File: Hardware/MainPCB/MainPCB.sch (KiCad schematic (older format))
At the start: 23 parts, among them Q1 FDS9926A, U1 BQ24075, U2 BQ29700, U3 TLV75533PDBV

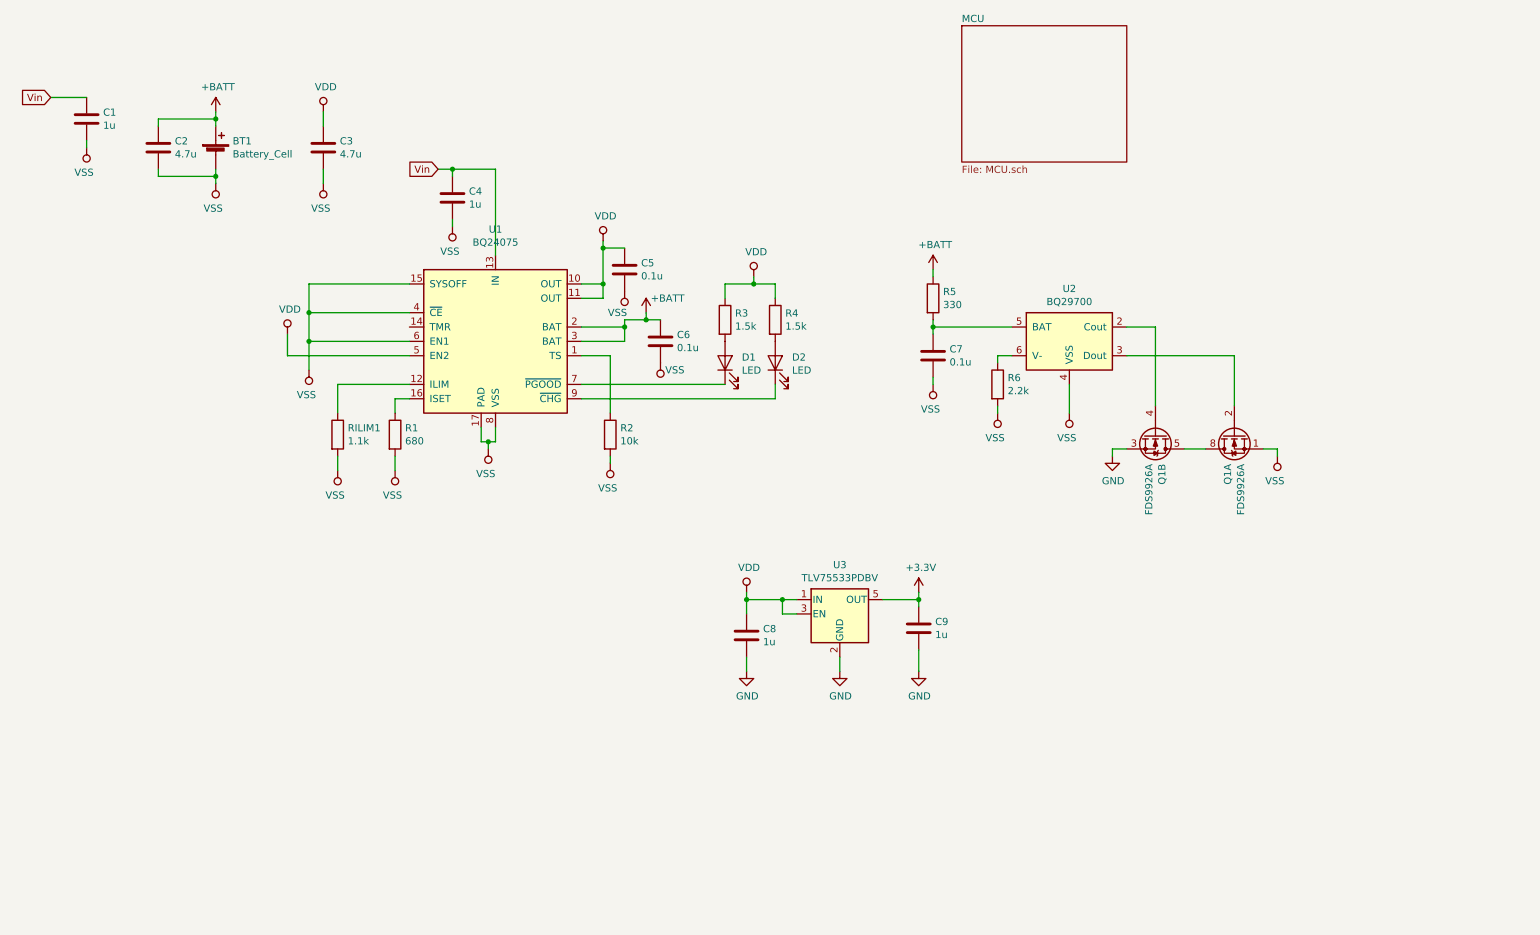
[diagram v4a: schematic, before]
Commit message: Discrete componenten rond IC's en IC's zelfs nagegaan. + toevoeging BOM
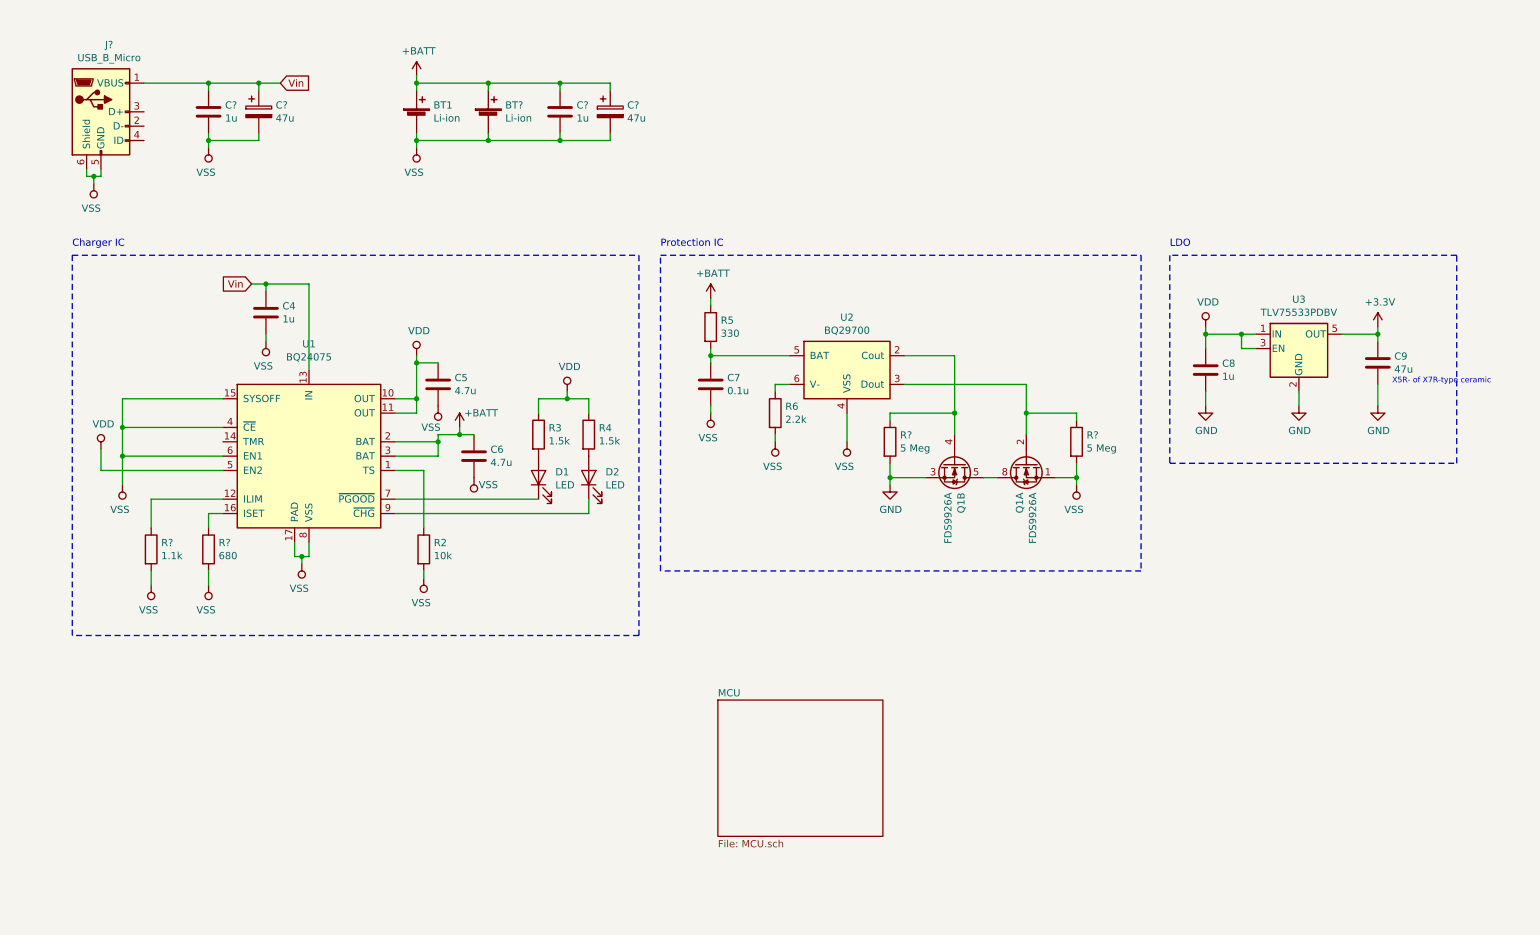
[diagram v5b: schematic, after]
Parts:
- removed C2, C3: 4.7u, symbol Device:C
- added BT?: Li-ion, Battery:BatteryHolder_Keystone_1042_1x18650, symbol Device:Battery_Cell
- added C? (x2): 47u, symbol Device:CP
- added C?: 1u, symbol Device:C
- added J?: USB_B_Micro, Connector_USB:USB_Micro-B_Wuerth_629105150521, symbol Connector:USB_B_Micro
- added R? (x2): 5 Meg, Resistor_SMD:R_0612_1632Metric, symbol Device:R
- BT1: value Battery_Cell -> Li-ion
- C5, C6: value 0.1u -> 4.7u
- C9: value 1u -> 47u
- renumbered C1 to C?, RILIM1 to R?, R1 to R?
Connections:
- net +BATT: now also BT?.1 (+), C?.1, C?.1
- net GND: now also R?.2
- net VSS: now also BT?.2 (-), C?.2, C?.2, C?.2, J?.5 (GND), J?.6 (Shield), R?.2
- net Vin: now also C?.1, J?.1 (VBUS)
- net at Q1.4 (G2), U2.2 (Cout): now also R?.1
- net at Q1.2 (G1), U2.3 (Dout): now also R?.1
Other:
- note added: "Charger IC"
- note added: "LDO"
- note added: "Protection IC"
- note added: "X5R- of X7R-type ceramic"
- moved on the sheet: BT1, C4, C5, C6, C7, C8, C9, C?, D1, D2, Q1A, Q1B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

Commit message: schematic voor esp32 mainboard
de esp toegevoegd en de nodige connecties gemaakt
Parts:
- U3: symbol Regulator_Linear:TLV75533PDBV -> MainPCB-rescue:TLV75533PDBV-Regulator_Linear
- gave numbers to parts that had none: 10
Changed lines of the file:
@@
 EESchema Schematic File Version 4
+LIBS:MainPCB-cache
 EELAYER 30 0
 EELAYER END
@@
 $EndComp
 $Comp
-L Device:R R?
+L Device:R R7
 U 1 1 5E5AB74D
 P 2000 4250
-F 0 "R?" H 2070 4296 50  0000 L CNN
+F 0 "R7" H 2070 4296 50  0000 L CNN
 F 1 "680" H 2070 4205 50  0000 L CNN
 F 2 "Resistor_SMD:R_0612_1632Metric" V 1930 4250 50  0001 C CNN
@@
 	1250 3700 1250 3550
 $Comp
-L Device:R R?
+L Device:R R1
 U 1 1 5E5A99E6
 P 1600 4250
-F 0 "R?" H 1670 4296 50  0000 L CNN
+F 0 "R1" H 1670 4296 50  0000 L CNN
 F 1 "1.1k" H 1670 4205 50  0000 L CNN
 F 2 "Resistor_SMD:R_0612_1632Metric" V 1530 4250 50  0001 C CNN
@@
 $EndComp
 $Comp
-L Device:C C?
+L Device:C C1
 U 1 1 5E64C3A1
 P 2000 1200
-F 0 "C?" H 2115 1246 50  0000 L CNN
+F 0 "C1" H 2115 1246 50  0000 L CNN
 F 1 "1u" H 2115 1155 50  0000 L CNN
 F 2 "" H 2038 1050 50  0001 C CNN
@@
 	6750 3800 6750 3750
 $Comp
-L Regulator_Linear:TLV75533PDBV U3
+L MainPCB-rescue:TLV75533PDBV-Regulator_Linear U3
 U 1 1 5E669F5C
 P 9600 2850
@@
 LDO
 $Comp
-L Device:Battery_Cell BT?
+L Device:Battery_Cell BT2
 U 1 1 5E66A880
 P 3950 1250
-F 0 "BT?" H 4068 1346 50  0000 L CNN
+F 0 "BT2" H 4068 1346 50  0000 L CNN
 F 1 "Li-ion" H 4068 1255 50  0000 L CNN
 F 2 "Battery:BatteryHolder_Keystone_1042_1x18650" V 3950 1310 50  0001 C CNN
@@
 	2000 1050 2000 1000
 $Comp
-L Device:CP C?
+L Device:CP C2
 U 1 1 5E67A43B
 P 2350 1200
-F 0 "C?" H 2468 1246 50  0000 L CNN
+F 0 "C2" H 2468 1246 50  0000 L CNN
 F 1 "47u" H 2468 1155 50  0000 L CNN
 F 2 "" H 2388 1050 50  0001 C CNN
@@
 X5R- of X7R-type ceramic
 $Comp
-L Device:R R?
+L Device:R R8
 U 1 1 5E692923
 P 6750 3500
-F 0 "R?" H 6820 3546 50  0000 L CNN
+F 0 "R8" H 6820 3546 50  0000 L CNN
 F 1 "5 Meg" H 6820 3455 50  0000 L CNN
 F 2 "Resistor_SMD:R_0612_1632Metric" V 6680 3500 50  0001 C CNN
@@
 	7200 3300 7200 3450
 $Comp
-L Device:R R?
+L Device:R R9
 U 1 1 5E6ADB8A
 P 8050 3500
-F 0 "R?" H 8120 3546 50  0000 L CNN
+F 0 "R9" H 8120 3546 50  0000 L CNN
 F 1 "5 Meg" H 8120 3455 50  0000 L CNN
 F 2 "Resistor_SMD:R_0612_1632Metric" V 7980 3500 50  0001 C CNN
@@
 	3450 1400 3950 1400
 $Comp
-L Connector:USB_B_Micro J?
+L Connector:USB_B_Micro J1
 U 1 1 5E6EC061
 P 1250 1200
-F 0 "J?" H 1307 1667 50  0000 C CNN
+F 0 "J1" H 1307 1667 50  0000 C CNN
 F 1 "USB_B_Micro" H 1307 1576 50  0000 C CNN
 F 2 "Connector_USB:USB_Micro-B_Wuerth_629105150521" H 1400 1150 50  0001 C CNN
@@
 	1550 1000 2000 1000
 $Comp
-L power:VSS #PWR?
+L power:VSS #PWR0101
 U 1 1 5E70438C
 P 1200 1700
-F 0 "#PWR?" H 1200 1550 50  0001 C CNN
+F 0 "#PWR0101" H 1200 1550 50  0001 C CNN
 F 1 "VSS" H 1218 1873 50  0000 C CNN
 F 2 "" H 1200 1700 50  0001 C CNN
@@
 Connection ~ 1200 1650
 $Comp
-L Device:C C?
+L Device:C C3
 U 1 1 5E71B7EF
 P 4450 1200
-F 0 "C?" H 4565 1246 50  0000 L CNN
+F 0 "C3" H 4565 1246 50  0000 L CNN
 F 1 "1u" H 4565 1155 50  0000 L CNN
 F 2 "" H 4488 1050 50  0001 C CNN
@@
 $EndComp
 $Comp
-L Device:CP C?
+L Device:CP C11
 U 1 1 5E71B7F5
 P 4800 1200
-F 0 "C?" H 4918 1246 50  0000 L CNN
+F 0 "C11" H 4918 1246 50  0000 L CNN
 F 1 "47u" H 4918 1155 50  0000 L CNN
 F 2 "" H 4838 1050 50  0001 C CNN

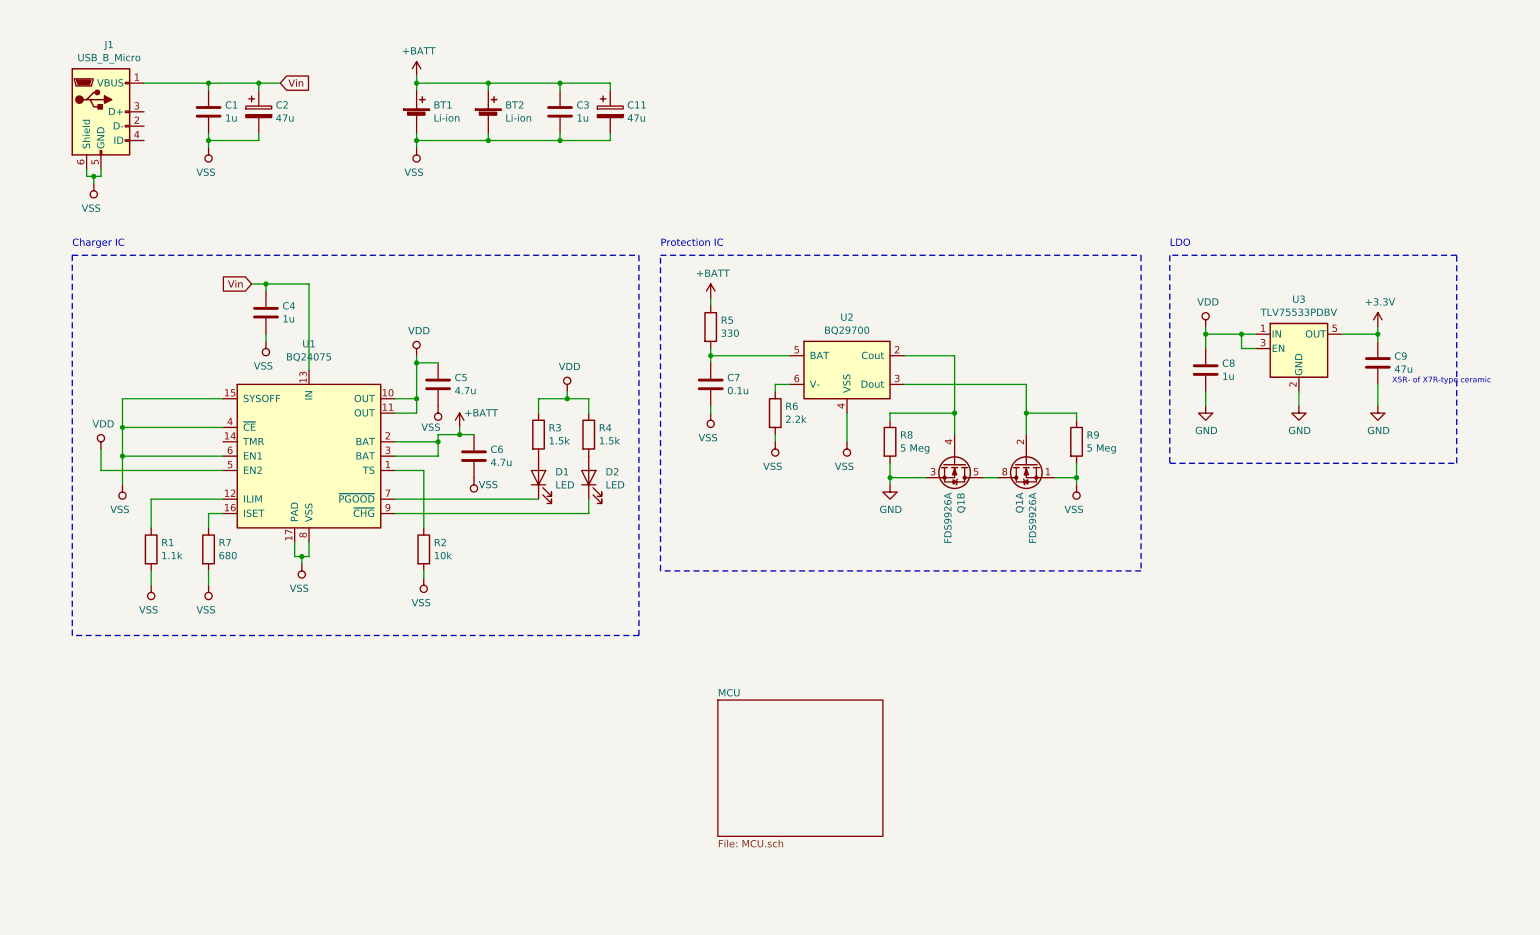
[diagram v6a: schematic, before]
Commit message: Main PCB volledig uitgerust met foorprints voor discrete componenten + BOM aangevuld met alles
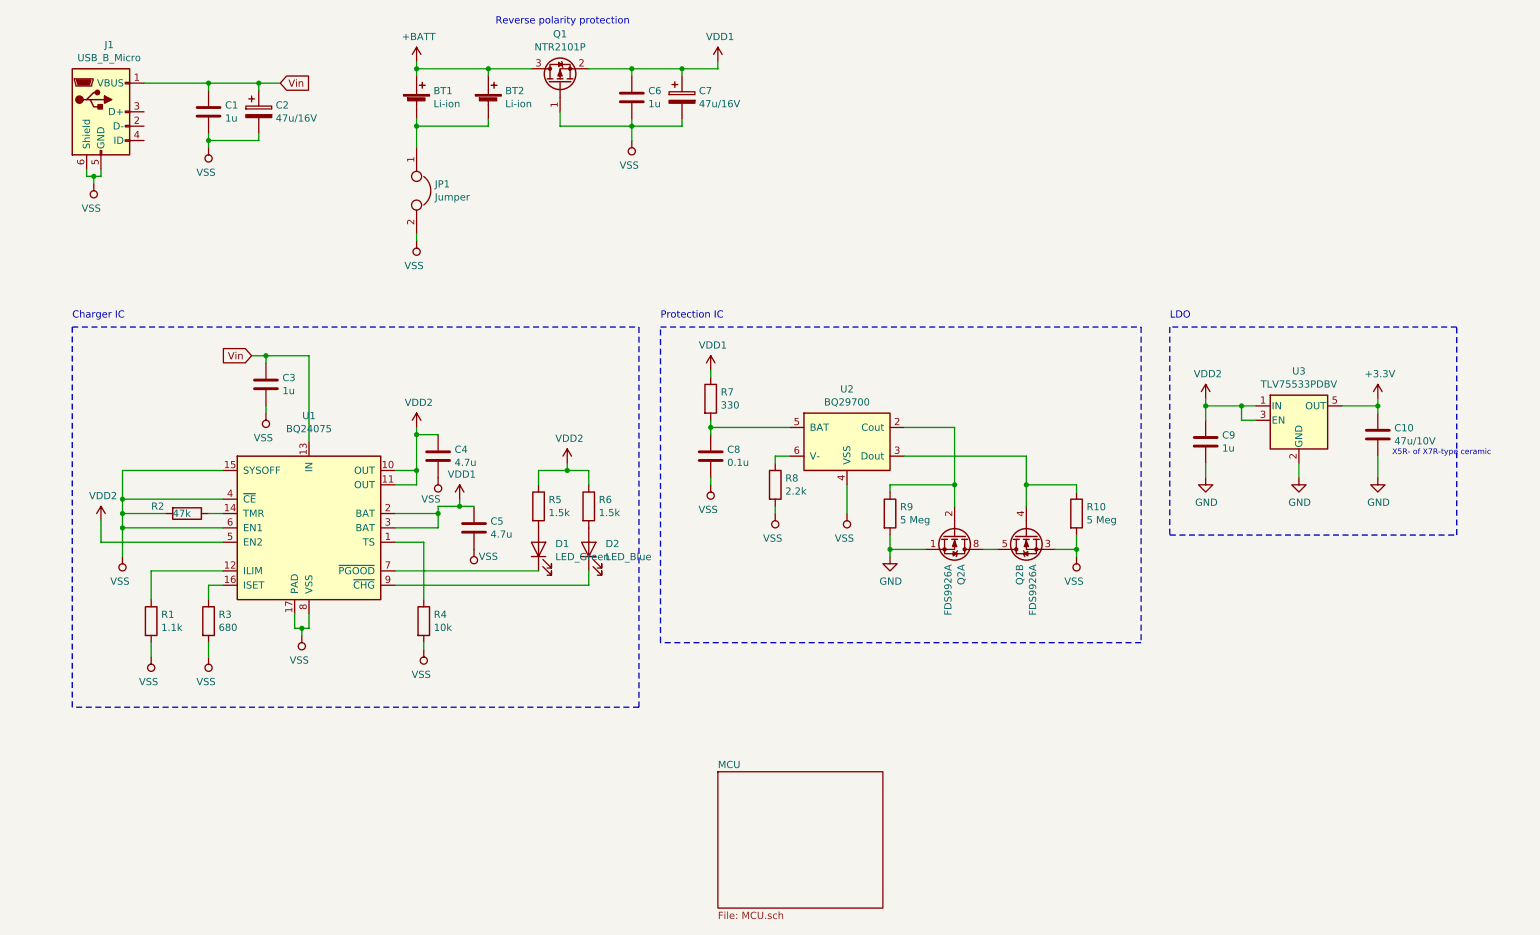
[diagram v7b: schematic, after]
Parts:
- removed C11: 47u, symbol Device:CP
- removed C3: 1u, symbol Device:C
- added C6: 1u, Capacitor_SMD:C_1206_3216Metric_Pad1.42x1.75mm_HandSolder, symbol Device:C
- added C7: 47u/16V, Capacitor_SMD:CP_Elec_5x5.4, symbol Device:CP
- added JP1: Jumper, Tobias_KiCad_Lib:Wire, symbol Device:Jumper
- added Q1: NTR2101P, Package_TO_SOT_SMD:SOT-23, symbol Transistor_FET:NTR2101P
- added R2: 47k, Resistor_SMD:R_1206_3216Metric_Pad1.42x1.75mm_HandSolder, symbol Device:R
- C1: footprint (none) -> Capacitor_SMD:C_1206_3216Metric_Pad1.42x1.75mm_HandSolder
- C10: renamed from C9; value 47u -> 47u/10V; footprint (none) -> Capacitor_SMD:C_1206_3216Metric_Pad1.42x1.75mm_HandSolder
- C2: value 47u -> 47u/16V; footprint (none) -> Capacitor_SMD:CP_Elec_5x5.4
- C3: renamed from C4; footprint (none) -> Capacitor_SMD:C_1206_3216Metric_Pad1.42x1.75mm_HandSolder
- C4: renamed from C5; footprint (none) -> Capacitor_SMD:C_1206_3216Metric_Pad1.42x1.75mm_HandSolder
- C5: renamed from C6; footprint (none) -> Capacitor_SMD:C_1206_3216Metric_Pad1.42x1.75mm_HandSolder
- C8: renamed from C7; footprint (none) -> Capacitor_SMD:C_1206_3216Metric_Pad1.42x1.75mm_HandSolder
- C9: renamed from C8; footprint (none) -> Capacitor_SMD:C_1206_3216Metric_Pad1.42x1.75mm_HandSolder
- D1: value LED -> LED_Green; footprint (none) -> LED_THT:LED_D3.0mm
- D2: value LED -> LED_Blue; footprint (none) -> LED_THT:LED_D3.0mm
- R1: footprint Resistor_SMD:R_0612_1632Metric -> Resistor_SMD:R_1206_3216Metric_Pad1.42x1.75mm_HandSolder
- R10: renamed from R9; footprint Resistor_SMD:R_0612_1632Metric -> Resistor_SMD:R_1206_3216Metric_Pad1.42x1.75mm_HandSolder
- R3: renamed from R7; footprint Resistor_SMD:R_0612_1632Metric -> Resistor_SMD:R_1206_3216Metric_Pad1.42x1.75mm_HandSolder
- R4: renamed from R2; footprint Resistor_SMD:R_0612_1632Metric -> Resistor_SMD:R_1206_3216Metric_Pad1.42x1.75mm_HandSolder
- R5: renamed from R3; footprint Resistor_SMD:R_0612_1632Metric -> Resistor_SMD:R_1206_3216Metric_Pad1.42x1.75mm_HandSolder
- R6: renamed from R4; footprint Resistor_SMD:R_0612_1632Metric -> Resistor_SMD:R_1206_3216Metric_Pad1.42x1.75mm_HandSolder
- R7: renamed from R5; footprint Resistor_SMD:R_0612_1632Metric -> Resistor_SMD:R_1206_3216Metric_Pad1.42x1.75mm_HandSolder
- R8: renamed from R6; footprint Resistor_SMD:R_0612_1632Metric -> Resistor_SMD:R_1206_3216Metric_Pad1.42x1.75mm_HandSolder
- R9: renamed from R8; footprint Resistor_SMD:R_0612_1632Metric -> Resistor_SMD:R_1206_3216Metric_Pad1.42x1.75mm_HandSolder
- renumbered Q1 to Q2
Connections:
- net +BATT: now also Q1.3 (D); no longer C5.1, R7.1, U1.2 (BAT), U1.3 (BAT)
- net GND: now also Q2.1 (S1); no longer Q2.3 (S2)
- net VSS: now also Q2.3 (S2), C6.2, C7.2, JP1.2, Q1.1 (G), R2.2; no longer BT1.2 (-), BT2.2 (-), Q2.1 (S1)
- net at U1.14 (TMR): now also R2.1
- net at R9.1, U2.2 (Cout): now also Q2.2 (G1); no longer Q2.4 (G2)
- net at R10.1, U2.3 (Dout): now also Q2.4 (G2); no longer Q2.2 (G1)
- net VDD renamed VDD2
- new net: Q2.5 (D2), Q2.6 (D2), Q2.7 (D1), Q2.8 (D1)
- new net: BT1.2 (-), BT2.2 (-), JP1.1
- new net VDD1: C5.1, C6.1, C7.1, Q1.2 (S), R7.1, U1.2 (BAT), U1.3 (BAT)
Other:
- note added: "Reverse polarity protection\n"
- moved on the sheet: BT1, BT2, C10, C3, C4, C5, C8, C9, D1, D2, R1, R10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

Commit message: Eerste plaatsing van componenten op PCB
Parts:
- JP1: value Jumper -> Stroommeetdraad
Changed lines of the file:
@@
 P 3450 1750
 F 0 "JP1" V 3404 1877 50  0000 L CNN
-F 1 "Jumper" V 3495 1877 50  0000 L CNN
+F 1 "Stroommeetdraad" V 3495 1877 50  0000 L CNN
 F 2 "Tobias_KiCad_Lib:Wire" H 3450 1750 50  0001 C CNN
 F 3 "~" H 3450 1750 50  0001 C CNN
